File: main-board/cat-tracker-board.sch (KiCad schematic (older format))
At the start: 38 parts, among them J1 Conn_01x10, J2 USB_C_Receptacle_USB2.0, J3 Conn_01x03, Q1 SI3443DDV-T1-GE3, Q2 Q_PNP_BCE, Q3 Q_NPN_BCE, Q4 SI3443DDV-T1-GE3, Q5 SI3443DDV-T1-GE3, U1 ATSAMD21E18A-A, U2 LM3480-3.3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

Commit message: Updated main board layout with battery board footprint.
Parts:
- BT1: footprint Battery:BatteryHolder_Keystone_2468_2xAAA -> cat-tracker-board:battery-board
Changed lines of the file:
@@
 F 0 "BT1" V 5555 4750 50  0000 C CNN
 F 1 "Battery" V 5646 4750 50  0000 C CNN
-F 2 "Battery:BatteryHolder_Keystone_2468_2xAAA" V 5800 4810 50  0001 C CNN
+F 2 "cat-tracker-board:battery-board" V 5800 4810 50  0001 C CNN
 F 3 "~" V 5800 4810 50  0001 C CNN
 	1    5800 4750

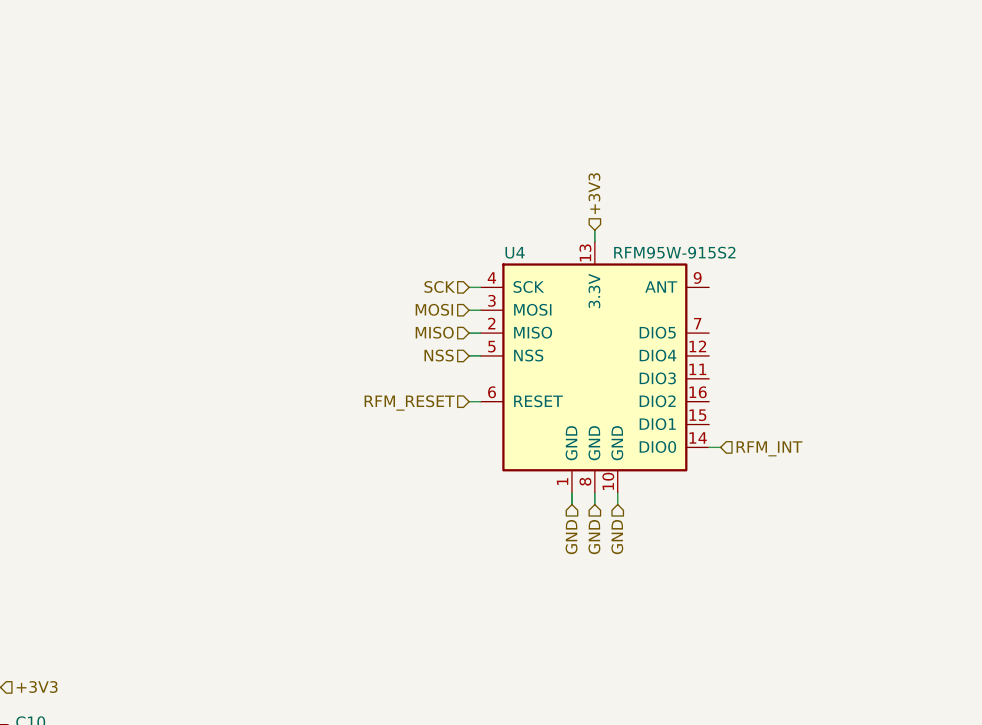
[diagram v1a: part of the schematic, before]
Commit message: Added lora antenna connector.
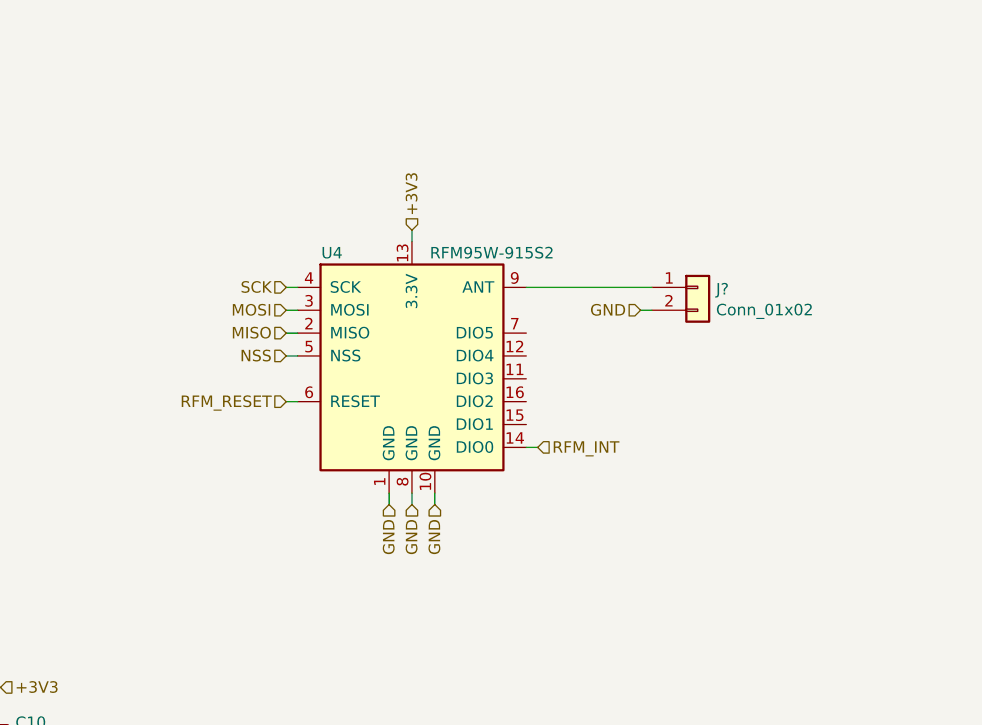
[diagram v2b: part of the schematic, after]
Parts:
- added J?: Conn_01x02, cat-tracker-board:RF-Solutions-CON-SMA-EDGE-S, symbol Connector_Generic:Conn_01x02
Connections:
- net GND: now also J?.2 (Pin_2)
- net at U4.9 (ANT): now also J?.1 (Pin_1)
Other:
- moved on the sheet: U4
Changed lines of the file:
@@
 L RF_Module:RFM95W-915S2 U4
 U 1 1 608B39CE
-P 14700 4550
-F 0 "U4" H 14350 5000 50  0000 C CNN
-F 1 "RFM95W-915S2" H 15050 5000 50  0000 C CNN
-F 2 "RF_Module:HOPERF_RFM9XW_SMD" H 11400 6200 50  0001 C CNN
-F 3 "https://www.hoperf.com/data/upload/portal/20181127/5bfcbea20e9ef.pdf" H 11400 6200 50  0001 C CNN
-F 4 "RF Solutions" H 14700 4550 50  0001 C CNN "mfg1"
-F 5 "RFM95W-915S2" H 14700 4550 50  0001 C CNN "mfg1pn"
-	1    14700 4550
+P 13900 4550
+F 0 "U4" H 13550 5000 50  0000 C CNN
+F 1 "RFM95W-915S2" H 14250 5000 50  0000 C CNN
+F 2 "RF_Module:HOPERF_RFM9XW_SMD" H 10600 6200 50  0001 C CNN
+F 3 "https://www.hoperf.com/data/upload/portal/20181127/5bfcbea20e9ef.pdf" H 10600 6200 50  0001 C CNN
+F 4 "RF Solutions" H 13900 4550 50  0001 C CNN "mfg1"
+F 5 "RFM95W-915S2" H 13900 4550 50  0001 C CNN "mfg1pn"
+	1    13900 4550
 	1    0    0    -1
 $EndComp
@@
 +3V3
 Wire Wire Line
-	14150 4750 14200 4750
-Wire Wire Line
-	14150 4550 14200 4550
-Wire Wire Line
-	14150 4450 14200 4450
-Wire Wire Line
-	14150 4350 14200 4350
-Wire Wire Line
-	14150 4250 14200 4250
-Wire Wire Line
-	14600 5200 14600 5150
-Wire Wire Line
-	14700 5200 14700 5150
-Wire Wire Line
-	14800 5200 14800 5150
-Wire Wire Line
-	14700 4000 14700 4050
-Text HLabel 14700 4000 1    50   Input ~ 0
+	13350 4750 13400 4750
+Wire Wire Line
+	13350 4550 13400 4550
+Wire Wire Line
+	13350 4450 13400 4450
+Wire Wire Line
+	13350 4350 13400 4350
+Wire Wire Line
+	13350 4250 13400 4250
+Wire Wire Line
+	13800 5200 13800 5150
+Wire Wire Line
+	13900 5200 13900 5150
+Wire Wire Line
+	14000 5200 14000 5150
+Wire Wire Line
+	13900 4000 13900 4050
+Text HLabel 13900 4000 1    50   Input ~ 0
 +3V3
-Text HLabel 14700 5200 3    50   Input ~ 0
-GND
-Text HLabel 14600 5200 3    50   Input ~ 0
-GND
-Text HLabel 14800 5200 3    50   Input ~ 0
-GND
-Text HLabel 14150 4250 0    50   Input ~ 0
+Text HLabel 13900 5200 3    50   Input ~ 0
+GND
+Text HLabel 13800 5200 3    50   Input ~ 0
+GND
+Text HLabel 14000 5200 3    50   Input ~ 0
+GND
+Text HLabel 13350 4250 0    50   Input ~ 0
 SCK
-Text HLabel 14150 4350 0    50   Input ~ 0
+Text HLabel 13350 4350 0    50   Input ~ 0
 MOSI
-Text HLabel 14150 4450 0    50   Input ~ 0
+Text HLabel 13350 4450 0    50   Input ~ 0
 MISO
-Text HLabel 14150 4550 0    50   Input ~ 0
+Text HLabel 13350 4550 0    50   Input ~ 0
 NSS
-Text HLabel 14150 4750 0    50   Input ~ 0
+Text HLabel 13350 4750 0    50   Input ~ 0
 RFM_RESET
 Wire Wire Line
-	15250 4950 15200 4950
-Text HLabel 15250 4950 2    50   Input ~ 0
+	14450 4950 14400 4950
+Text HLabel 14450 4950 2    50   Input ~ 0
 RFM_INT
 Wire Wire Line
@@
 Wire Wire Line
 	12850 7700 12950 7700
+$Comp
+L Connector_Generic:Conn_01x02 J?
+U 1 1 608E9ABB
+P 15150 4250
+F 0 "J?" H 15230 4242 50  0000 L CNN
+F 1 "Conn_01x02" H 15230 4151 50  0000 L CNN
+F 2 "cat-tracker-board:RF-Solutions-CON-SMA-EDGE-S" H 15150 4250 50  0001 C CNN
+F 3 "~" H 15150 4250 50  0001 C CNN
+F 4 "RF Solutions" H 15150 4250 50  0001 C CNN "mfg1"
+F 5 "CON-SMA-EDGE-S" H 15150 4250 50  0001 C CNN "mfg1pn"
+	1    15150 4250
+	1    0    0    -1
+$EndComp
+Wire Wire Line
+	14950 4350 14900 4350
+Text HLabel 14900 4350 0    50   Input ~ 0
+GND
+Wire Wire Line
+	14400 4250 14950 4250
 $EndSCHEMATC

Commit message: Assigned remaining main-board part numbers.
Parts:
- C1: mfg1 (none) -> Samsung Electro-Mechanics; mfg1pn (none) -> CL21B105KBFNNNG
- C3, C5, C6, C7, C8: mfg1 (none) -> AVX; mfg1pn (none) -> 08055C104KAT2A
- FB1: mfg1 (none) -> Murata Electronics; mfg1pn (none) -> BLM21AG151SN1D
- J1: mfg1 (none) -> Samtec; mfg1pn (none) -> FTSH-105-01-F-D-K
- J3: mfg1 (none) -> JST Sales America; mfg1pn (none) -> S3B-PH-K-S(LF)(SN)
- R1, R2, R3, R5, R8: mfg1 (none) -> Vishay / Dale; mfg1pn (none) -> CRCW0805100KJNEAC
- R10, R9: mfg1 (none) -> Yageo; mfg1pn (none) -> RC0805JR-075K1L
- R4: mfg1 (none) -> Panasonic; mfg1pn (none) -> ERJ-6GEYJ274V
- R6, R7: value 500k -> 510k; mfg1 (none) -> Panasonic; mfg1pn (none) -> ERJ-6GEYJ514V
- U1: mfg1 (none) -> Microchip; mfg1pn (none) -> ATSAMD21E18A-AU
- gave numbers to parts that had none: 1
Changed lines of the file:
@@
 F 2 "Capacitor_SMD:C_0805_2012Metric" H 1888 2550 50  0001 C CNN
 F 3 "~" H 1850 2700 50  0001 C CNN
+F 4 "Samsung Electro-Mechanics" H 1850 2700 50  0001 C CNN "mfg1"
+F 5 "CL21B105KBFNNNG" H 1850 2700 50  0001 C CNN "mfg1pn"
 	1    1850 2700
 	0    -1   1    0
@@
 F 2 "Capacitor_SMD:C_0805_2012Metric" H 2888 2550 50  0001 C CNN
 F 3 "~" H 2850 2700 50  0001 C CNN
+F 4 "AVX" H 2850 2700 50  0001 C CNN "mfg1"
+F 5 "08055C104KAT2A" H 2850 2700 50  0001 C CNN "mfg1pn"
 	1    2850 2700
 	0    1    1    0
@@
 F 2 "Inductor_SMD:L_0805_2012Metric" V 2780 1800 50  0001 C CNN
 F 3 "~" H 2850 1800 50  0001 C CNN
+F 4 "Murata Electronics" H 2850 1800 50  0001 C CNN "mfg1"
+F 5 "BLM21AG151SN1D" H 2850 1800 50  0001 C CNN "mfg1pn"
 	1    2850 1800
 	0    1    1    0
@@
 F 2 "Capacitor_SMD:C_0805_2012Metric" H 2088 2100 50  0001 C CNN
 F 3 "~" H 2050 2250 50  0001 C CNN
+F 4 "AVX" H 2050 2250 50  0001 C CNN "mfg1"
+F 5 "08055C104KAT2A" H 2050 2250 50  0001 C CNN "mfg1pn"
 	1    2050 2250
 	0    -1   1    0
@@
 F 2 "Connector_PinHeader_1.27mm:PinHeader_2x05_P1.27mm_Vertical" H 5500 2300 50  0001 C CNN
 F 3 "~" H 5500 2300 50  0001 C CNN
+F 4 "Samtec" H 5500 2300 50  0001 C CNN "mfg1"
+F 5 "FTSH-105-01-F-D-K" H 5500 2300 50  0001 C CNN "mfg1pn"
 	1    5500 2300
 	1    0    0    -1
@@
 F 2 "Resistor_SMD:R_0805_2012Metric" V 4780 1800 50  0001 C CNN
 F 3 "~" H 4850 1800 50  0001 C CNN
+F 4 "Vishay / Dale" H 4850 1800 50  0001 C CNN "mfg1"
+F 5 "CRCW0805100KJNEAC" H 4850 1800 50  0001 C CNN "mfg1pn"
 	1    4850 1800
 	-1   0    0    -1
@@
 F 2 "Resistor_SMD:R_0805_2012Metric" V 4280 2400 50  0001 C CNN
 F 3 "~" H 4350 2400 50  0001 C CNN
+F 4 "Vishay / Dale" H 4350 2400 50  0001 C CNN "mfg1"
+F 5 "CRCW0805100KJNEAC" H 4350 2400 50  0001 C CNN "mfg1pn"
 	1    4350 2400
 	-1   0    0    -1
@@
 F 2 "Package_QFP:TQFP-32_7x7mm_P0.8mm" H 3250 2900 50  0001 C CNN
 F 3 "http://ww1.microchip.com/downloads/en/DeviceDoc/SAM_D21_DA1_Family_Data%20Sheet_DS40001882E.pdf" H 2350 4750 50  0001 C CNN
+F 4 "Microchip" H 2350 4750 50  0001 C CNN "mfg1"
+F 5 "ATSAMD21E18A-AU" H 2350 4750 50  0001 C CNN "mfg1pn"
 	1    2350 4750
 	1    0    0    -1
@@
 F 2 "Resistor_SMD:R_0805_2012Metric" V 13680 1350 50  0001 C CNN
 F 3 "~" H 13750 1350 50  0001 C CNN
+F 4 "Yageo" H 13750 1350 50  0001 C CNN "mfg1"
+F 5 "RC0805JR-075K1L" H 13750 1350 50  0001 C CNN "mfg1pn"
 	1    13750 1350
 	0    1    1    0
@@
 F 2 "Resistor_SMD:R_0805_2012Metric" V 13680 1450 50  0001 C CNN
 F 3 "~" H 13750 1450 50  0001 C CNN
+F 4 "Yageo" H 13750 1450 50  0001 C CNN "mfg1"
+F 5 "RC0805JR-075K1L" H 13750 1450 50  0001 C CNN "mfg1pn"
 	1    13750 1450
 	0    1    1    0
@@
 F 2 "Capacitor_SMD:C_0805_2012Metric" H 9088 2100 50  0001 C CNN
 F 3 "~" H 9050 2250 50  0001 C CNN
+F 4 "AVX" H 9050 2250 50  0001 C CNN "mfg1"
+F 5 "08055C104KAT2A" H 9050 2250 50  0001 C CNN "mfg1pn"
 	1    9050 2250
 	1    0    0    1
@@
 F 2 "Capacitor_SMD:C_0805_2012Metric" H 9788 2100 50  0001 C CNN
 F 3 "~" H 9750 2250 50  0001 C CNN
+F 4 "AVX" H 9750 2250 50  0001 C CNN "mfg1"
+F 5 "08055C104KAT2A" H 9750 2250 50  0001 C CNN "mfg1pn"
 	1    9750 2250
 	1    0    0    1
@@
 F 2 "Resistor_SMD:R_0805_2012Metric" V 6830 5300 50  0001 C CNN
 F 3 "~" H 6900 5300 50  0001 C CNN
+F 4 "Vishay / Dale" H 6900 5300 50  0001 C CNN "mfg1"
+F 5 "CRCW0805100KJNEAC" H 6900 5300 50  0001 C CNN "mfg1pn"
 	1    6900 5300
 	-1   0    0    -1
@@
 P 9000 5150
 F 0 "R6" H 9070 5196 50  0000 L CNN
-F 1 "500k" H 9070 5105 50  0000 L CNN
+F 1 "510k" H 9070 5105 50  0000 L CNN
 F 2 "Resistor_SMD:R_0805_2012Metric" V 8930 5150 50  0001 C CNN
 F 3 "~" H 9000 5150 50  0001 C CNN
+F 4 "Panasonic" H 9000 5150 50  0001 C CNN "mfg1"
+F 5 "ERJ-6GEYJ514V" H 9000 5150 50  0001 C CNN "mfg1pn"
 	1    9000 5150
 	1    0    0    -1
@@
 F 2 "Resistor_SMD:R_0805_2012Metric" V 8480 5700 50  0001 C CNN
 F 3 "~" H 8550 5700 50  0001 C CNN
+F 4 "Panasonic" H 8550 5700 50  0001 C CNN "mfg1"
+F 5 "ERJ-6GEYJ274V" H 8550 5700 50  0001 C CNN "mfg1pn"
 	1    8550 5700
 	1    0    0    -1
@@
 F 2 "Resistor_SMD:R_0805_2012Metric" V 8480 6100 50  0001 C CNN
 F 3 "~" H 8550 6100 50  0001 C CNN
+F 4 "Vishay / Dale" H 8550 6100 50  0001 C CNN "mfg1"
+F 5 "CRCW0805100KJNEAC" H 8550 6100 50  0001 C CNN "mfg1pn"
 	1    8550 6100
 	1    0    0    -1
@@
 P 9350 5150
 F 0 "R7" H 9420 5196 50  0000 L CNN
-F 1 "500k" H 9420 5105 50  0000 L CNN
+F 1 "510k" H 9420 5105 50  0000 L CNN
 F 2 "Resistor_SMD:R_0805_2012Metric" V 9280 5150 50  0001 C CNN
 F 3 "~" H 9350 5150 50  0001 C CNN
+F 4 "Panasonic" H 9350 5150 50  0001 C CNN "mfg1"
+F 5 "ERJ-6GEYJ514V" H 9350 5150 50  0001 C CNN "mfg1pn"
 	1    9350 5150
 	1    0    0    -1
@@
 F 2 "Capacitor_SMD:C_0805_2012Metric" H 8388 5350 50  0001 C CNN
 F 3 "~" H 8350 5500 50  0001 C CNN
+F 4 "AVX" H 8350 5500 50  0001 C CNN "mfg1"
+F 5 "08055C104KAT2A" H 8350 5500 50  0001 C CNN "mfg1pn"
 	1    8350 5500
 	0    1    1    0
@@
 F 2 "Connector_JST:JST_PH_S3B-PH-K_1x03_P2.00mm_Horizontal" H 15000 7850 50  0001 C CNN
 F 3 "~" H 15000 7850 50  0001 C CNN
+F 4 "JST Sales America" H 15000 7850 50  0001 C CNN "mfg1"
+F 5 "S3B-PH-K-S(LF)(SN)" H 15000 7850 50  0001 C CNN "mfg1pn"
 	1    15000 7850
 	1    0    0    -1
@@
 F 2 "Resistor_SMD:R_0805_2012Metric" V 12980 7450 50  0001 C CNN
 F 3 "~" H 13050 7450 50  0001 C CNN
+F 4 "Vishay / Dale" H 13050 7450 50  0001 C CNN "mfg1"
+F 5 "CRCW0805100KJNEAC" H 13050 7450 50  0001 C CNN "mfg1pn"
 	1    13050 7450
 	0    -1   1    0
@@
 	12850 7700 12950 7700
 $Comp
-L Connector_Generic:Conn_01x02 J?
+L Connector_Generic:Conn_01x02 J4
 U 1 1 608E9ABB
 P 15150 4250
-F 0 "J?" H 15230 4242 50  0000 L CNN
+F 0 "J4" H 15230 4242 50  0000 L CNN
 F 1 "Conn_01x02" H 15230 4151 50  0000 L CNN
 F 2 "cat-tracker-board:RF-Solutions-CON-SMA-EDGE-S" H 15150 4250 50  0001 C CNN

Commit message: Changed programming header to right angle and updated pcb.
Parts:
- J1: footprint Connector_PinHeader_1.27mm:PinHeader_2x05_P1.27mm_Vertical -> Connector_PinHeader_1.27mm:PinHeader_2x05_P1.27mm_Horizontal; mfg1pn FTSH-105-01-F-D-K -> FTSH-105-01-F-D-RA-K
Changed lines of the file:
@@
 F 0 "J1" H 5418 2917 50  0000 C CNN
 F 1 "Conn_01x10" H 5418 2826 50  0000 C CNN
-F 2 "Connector_PinHeader_1.27mm:PinHeader_2x05_P1.27mm_Vertical" H 5500 2300 50  0001 C CNN
+F 2 "Connector_PinHeader_1.27mm:PinHeader_2x05_P1.27mm_Horizontal" H 5500 2300 50  0001 C CNN
 F 3 "~" H 5500 2300 50  0001 C CNN
 F 4 "Samtec" H 5500 2300 50  0001 C CNN "mfg1"
-F 5 "FTSH-105-01-F-D-K" H 5500 2300 50  0001 C CNN "mfg1pn"
+F 5 "FTSH-105-01-F-D-RA-K" H 5500 2300 50  0001 C CNN "mfg1pn"
 	1    5500 2300
 	1    0    0    -1

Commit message: Placed all parts on board.
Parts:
- added D4: PRTR5V0U2X, Package_TO_SOT_SMD:SOT-143, symbol Power_Protection:PRTR5V0U2X
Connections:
- net GND: now also D4.1 (GND)
- net RFM_INT: now also U1.15 (PA14); no longer U1.3 (PA02)
- net RFM_RESET: now also U1.16 (PA15); no longer U1.4 (PA03)
- net USBDM: now also D4.2 (I/O1)
- net USBDP: now also D4.3 (I/O2)
- net VUSB: now also D4.4 (VCC)
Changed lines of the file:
@@
 RFM_INT
 Wire Wire Line
-	1600 3450 1650 3450
+	1600 4650 1650 4650
 Wire Wire Line
 	1600 4150 1650 4150
@@
 Text HLabel 1600 4150 0    50   Input ~ 0
 NSS
-Text HLabel 1600 3450 0    50   Input ~ 0
+Text HLabel 1600 4650 0    50   Input ~ 0
 RFM_RESET
 Wire Wire Line
@@
 Wire Wire Line
 	4350 2800 5300 2800
-Text HLabel 1600 3350 0    50   Input ~ 0
+Text HLabel 1600 4550 0    50   Input ~ 0
 RFM_INT
 Wire Wire Line
-	1600 3350 1650 3350
+	1600 4550 1650 4550
 Wire Wire Line
 	2350 6650 2350 6700
@@
 Wire Wire Line
 	14400 4250 14950 4250
+Wire Wire Line
+	11800 1250 11800 1300
+Text HLabel 11800 1250 1    50   Input ~ 0
+VUSB
+Wire Wire Line
+	11800 2300 11800 2350
+Text HLabel 11800 2350 3    50   Input ~ 0
+GND
+Wire Wire Line
+	12350 1800 12300 1800
+Text HLabel 12350 1800 2    50   Input ~ 0
+USBDP
+Wire Wire Line
+	11250 1800 11300 1800
+Text HLabel 11250 1800 0    50   Input ~ 0
+USBDM
+$Comp
+L Power_Protection:PRTR5V0U2X D4
+U 1 1 608FDA26
+P 11800 1800
+F 0 "D4" H 12344 1846 50  0000 L CNN
+F 1 "PRTR5V0U2X" H 12344 1755 50  0000 L CNN
+F 2 "Package_TO_SOT_SMD:SOT-143" H 11860 1800 50  0001 C CNN
+F 3 "https://assets.nexperia.com/documents/data-sheet/PRTR5V0U2X.pdf" H 11860 1800 50  0001 C CNN
+F 4 "Nexperia" H 11800 1800 50  0001 C CNN "mfg1"
+F 5 "PRTR5V0U2X,215" H 11800 1800 50  0001 C CNN "mfg1pn"
+	1    11800 1800
+	1    0    0    -1
+$EndComp
 $EndSCHEMATC

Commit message: Rescued ferrite bead (again?).
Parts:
- FB1: symbol Device:Ferrite_Bead -> cat-tracker-board-rescue:Ferrite_Bead-Device
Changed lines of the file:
@@
 GND
 $Comp
-L Device:Ferrite_Bead FB1
+L cat-tracker-board-rescue:Ferrite_Bead-Device FB1
 U 1 1 608B69C1
 P 2850 1800
